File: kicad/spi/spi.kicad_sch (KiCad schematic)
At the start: 18 parts, among them J1 Board Connector, J2 SPI 1, J3 IO Select, J4 SPI 2, J5 SPI 3, U1 TinyFPGA w/SPI Module, U2 TSR1-2433E, U3 SN74LVC8T245PWR, U4 SN74LVC8T245PWR, U5 FM25V05-G

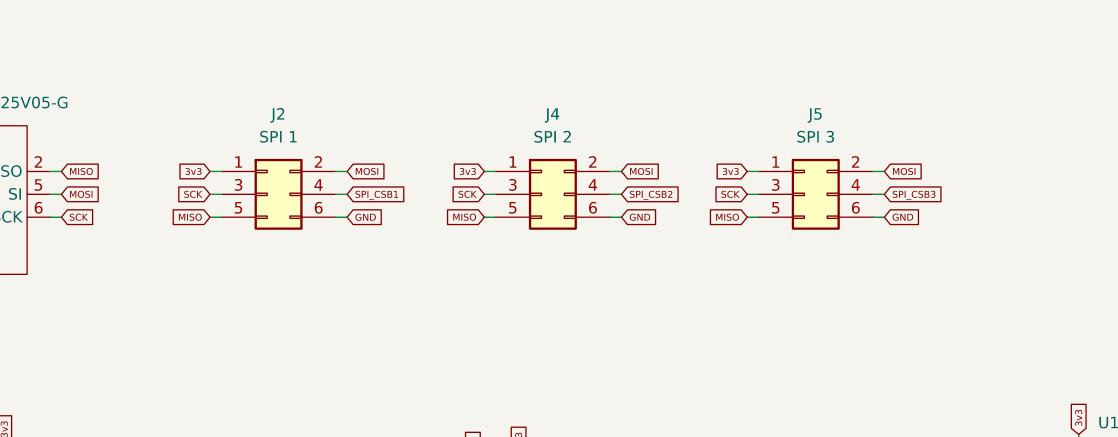
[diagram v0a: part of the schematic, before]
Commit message: setup eventual console output
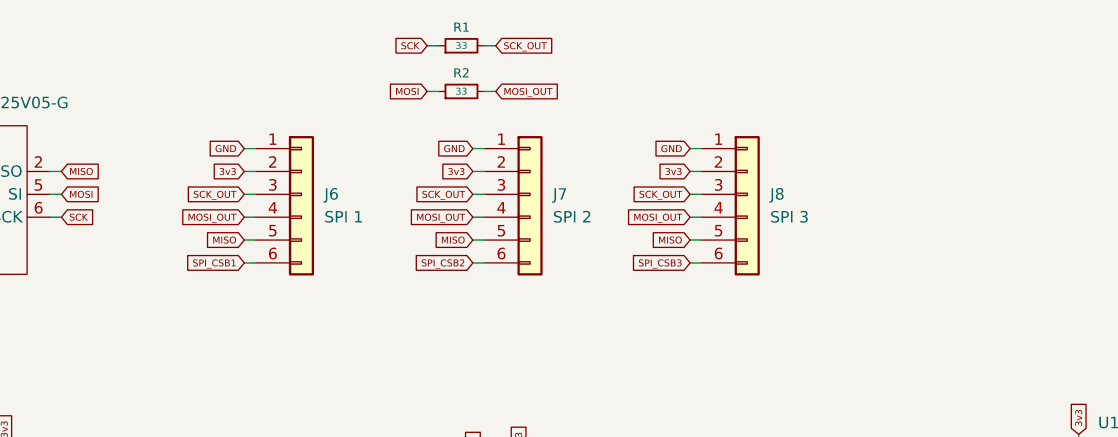
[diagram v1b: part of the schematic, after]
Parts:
- removed J2: SPI 1, Connector_IDC:IDC-Header_2x03_P2.54mm_Vertical, symbol Connector_Generic:Conn_02x03_Odd_Even
- removed J4: SPI 2, Connector_IDC:IDC-Header_2x03_P2.54mm_Vertical, symbol Connector_Generic:Conn_02x03_Odd_Even
- removed J5: SPI 3, Connector_IDC:IDC-Header_2x03_P2.54mm_Vertical, symbol Connector_Generic:Conn_02x03_Odd_Even
- added J6: SPI 1, Connector_JST:JST_PH_B6B-PH-K_1x06_P2.00mm_Vertical, symbol Connector_Generic:Conn_01x06
- added J7: SPI 2, Connector_JST:JST_PH_B6B-PH-K_1x06_P2.00mm_Vertical, symbol Connector_Generic:Conn_01x06
- added J8: SPI 3, Connector_JST:JST_PH_B6B-PH-K_1x06_P2.00mm_Vertical, symbol Connector_Generic:Conn_01x06
- added R1, R2: 33, Resistor_SMD:R_0603_1608Metric, symbol Device:R_Small
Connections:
- net 3v3: now also J6.2 (Pin_2), J7.2 (Pin_2), J8.2 (Pin_2)
- net GND: now also J6.1 (Pin_1), J7.1 (Pin_1), J8.1 (Pin_1)
- net MISO: now also J6.5 (Pin_5), J7.5 (Pin_5), J8.5 (Pin_5)
- net MOSI: now also R2.1
- net SCK: now also R1.1
- net SPI_CSB1: now also J6.6 (Pin_6)
- net SPI_CSB2: now also J7.6 (Pin_6)
- net SPI_CSB3: now also J8.6 (Pin_6)
- new net MOSI_OUT: J6.4 (Pin_4), J7.4 (Pin_4), J8.4 (Pin_4), R2.2
- new net SCK_OUT: J6.3 (Pin_3), J7.3 (Pin_3), J8.3 (Pin_3), R1.2

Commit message: added spi and via boards
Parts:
- J6, J7, J8: footprint Connector_JST:JST_PH_B6B-PH-K_1x06_P2.00mm_Vertical -> Connector_JST:JST_XH_B6B-XH-AM_1x06_P2.50mm_Vertical
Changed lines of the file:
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@@
 			)
 		)
-		(property "Footprint" "Connector_JST:JST_PH_B6B-PH-K_1x06_P2.00mm_Vertical"
+		(property "Footprint" "Connector_JST:JST_XH_B6B-XH-AM_1x06_P2.50mm_Vertical"
 			(at 152.4 46.99 0)
 			(hide yes)
@@
 			)
 		)
-		(property "Footprint" "Connector_JST:JST_PH_B6B-PH-K_1x06_P2.00mm_Vertical"
+		(property "Footprint" "Connector_JST:JST_XH_B6B-XH-AM_1x06_P2.50mm_Vertical"
 			(at 128.27 46.99 0)
 			(hide yes)
@@
 			)
 		)
-		(property "Footprint" "Connector_JST:JST_PH_B6B-PH-K_1x06_P2.00mm_Vertical"
+		(property "Footprint" "Connector_JST:JST_XH_B6B-XH-AM_1x06_P2.50mm_Vertical"
 			(at 102.87 46.99 0)
 			(hide yes)
